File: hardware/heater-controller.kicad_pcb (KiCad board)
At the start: 2 copper layers, 65 x 63 mm, 12 parts, among them J1 Vitotronic plug 96, Q1 SFH 309 FA

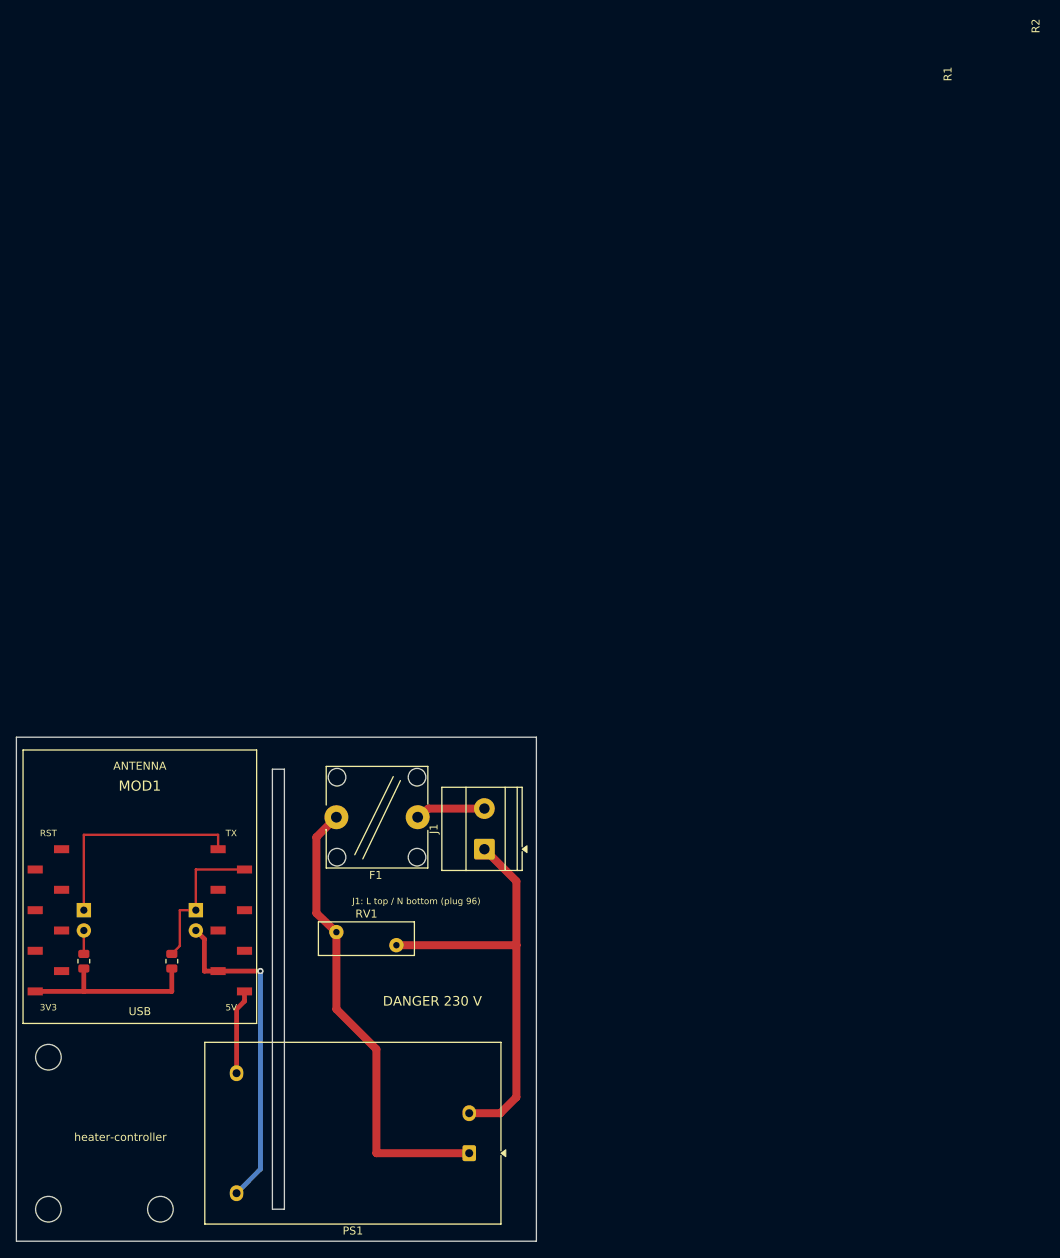
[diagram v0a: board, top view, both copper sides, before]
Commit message: feat(hardware): move to ESP32-C3 on a removable U-shaped board (#1)
* feat(hardware): move to ESP32-C3 on a removable U-shaped board

- ESP32-C3 super mini replaces the D1 mini: Optolink UART on GPIO4/GPIO3,
  logs over native USB
- inverted U board (86 x 39.5 mm): 230 V leg, optical head header on the bar,
  C3 on SMD female sockets; screw terminal for the mains wires
- off-board optical head on a 4-wire ribbon
- back GND pour, 0.7 mm power tracks, 6 mm mains isolation checked by DRC
- C3 socket footprint generator and fabrication export script
- enclosure redrawn around the new board

* feat(hardware): hand-solderable board with SMD C3 sockets for JLCPCB

- C3 plugged into two hanxia 1x8 SMD sockets (J3/J4) at 15.24 mm, the only
  parts with an LCSC number; MOD1 off board with a board-only outline
- through-hole everything else: TR5 T1A fuse, 07D431K varistor, JST PH
  vertical optical head connector, axial resistors
- HLK-PM01 footprint from the Hi-Link datasheet (15.4 / 29.4 mm pin pitch)
- footprints generated by footprints.py from the datasheets
- export adds the JLCPCB BOM and placement files
- routing done in KiCad: 0.7 mm power tracks, no ground plane

* feat(hardware): source every part at LCSC with datasheet footprints

- Kefa KF128 terminal block (Phoenix MKDS out of stock), Bourns MOV-07D431K
  inline varistor and JST PH with 0.9 mm holes, drawn by footprints.py
- LCSC number on every part; split-bom.py writes the JLCPCB BOM (SMD only)
  and an LCSC cart for the hand-soldered parts
- RV1 rerouted for its inline leads; DRC clean, schematic parity
- Enclosure split into named bodies: shells, lid, optical plug
- READMEs: parts list with suppliers, prices and footprint specs
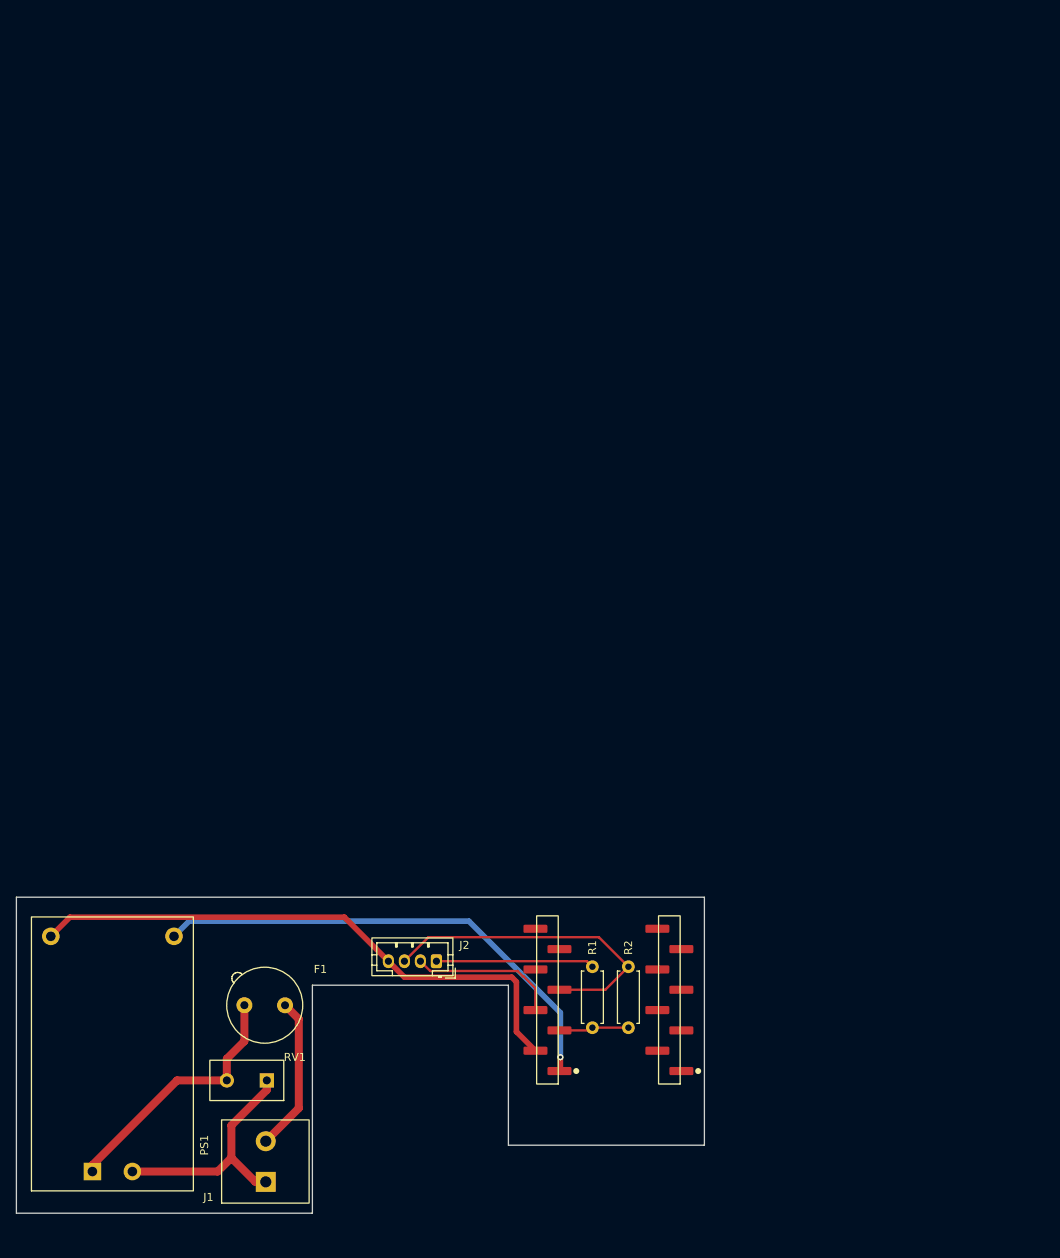
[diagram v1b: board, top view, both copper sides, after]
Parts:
- removed D1: SIR 204 EVL (IR), LED_THT:LED_D3.0mm_IRBlack
- removed H1, H2, H3: MountingHole_3.2mm_M3, MountingHole:MountingHole_3.2mm_M3
- removed Q1: SFH 309 FA, LED_THT:LED_D3.0mm_Clear
- added J2: JST B4B-PH-K (optical head), heater-controller:JST_PH_B4B-PH-K_1x04_P2.00mm_Vertical_Drill0.9, F.Cu at (152.5, 108.0)
- added J3: Socket 1x8 SMD (C3 pins 1-8), heater-controller:PinSocket_1x08_P2.54mm_SMD_HX-ZQ, F.Cu at (166.4, 112.8)
- added J4: Socket 1x8 SMD (C3 pins 9-16), heater-controller:PinSocket_1x08_P2.54mm_SMD_HX-ZQ, F.Cu at (181.6, 112.8)
- F1: value T500mA -> TR5 holder + T1A fuse; footprint Fuse:Fuseholder_Cylinder-5x20mm_Bulgin_FX0456_Vertical_Closed -> Fuse:Fuseholder_TR5_Littelfuse_No560_No460
- J1: value Vitotronic plug 96 -> KF128-5.08 (plug 96); footprint TerminalBlock_Phoenix:TerminalBlock_Phoenix_MKDS-1,5-2-5.08_1x02_P5.08mm_Horizontal -> heater-controller:TerminalBlock_Kefa_KF128-5.08_1x02
- MOD1: value WeMos_D1_mini -> ESP32-C3_SuperMini; footprint heater-controller:WEMOS_D1_mini_SMD_sockets -> heater-controller:ESP32-C3_SuperMini_Outline
- PS1: footprint Converter_ACDC:Converter_ACDC_Hi-Link_HLK-PMxx -> heater-controller:Converter_ACDC_HLK-PM01
- R1, R2: footprint Resistor_SMD:R_0805_2012Metric -> Resistor_THT:R_Axial_DIN0207_L6.3mm_D2.5mm_P7.62mm_Horizontal
- RV1: value 10D561K -> MOV-07D431K (275VAC); footprint Varistor:RV_Disc_D12mm_W4.2mm_P7.5mm -> heater-controller:RV_Disc_D9mm_W4.8mm_P5mm_Inline
- moved R1 64.1 mm to (172.0, 116.3)
- moved MOD1 59.3 mm to (174.0, 112.0), turned to 180 degrees
- moved R2 57.7 mm to (176.5, 116.3)
- moved J1 49.8 mm to (131.2, 135.6)
- moved PS1 47.2 mm to (109.5, 134.3), turned to 90 degrees
- moved F1 28.8 mm to (133.6, 113.5)
- moved RV1 23.4 mm to (131.3, 122.9)
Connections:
- R1 pad 2: Net-(D1-A) -> /LED_A
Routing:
- net +5V: track 10.6 -> 61.0 mm, vias 0 -> 1
- net GND: track 41.5 -> 72.1 mm, vias 1 -> 0
- net /TX_GPIO1: track 28.0 -> 0.00 mm
- net /L_FUSED: track 57.8 -> 32.3 mm
- net /N: track 54.4 -> 30.1 mm
- net /RX_GPIO3: track 19.0 -> 40.6 mm
- net /LED_A: track 0.00 -> 19.8 mm
- net /TX_GPIO4: track 0.00 -> 18.7 mm
- net /3V3: track 22.8 -> 8.76 mm
- net /L: track 8.72 -> 19.4 mm
- net Net-(D1-A): track 2.93 -> 0.00 mm
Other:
- board size 65 x 63 mm -> 86 x 39.5 mm
- board text removed: "DANGER 230 V"
- board text removed: "J1: L top / N bottom (plug 96)"
- board text removed: "OPTOLINK"
- board text removed: "RX"
- board text removed: "TX (IR LED)"
- board text removed: "heater-controller"
